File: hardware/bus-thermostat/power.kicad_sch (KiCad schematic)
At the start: 14 parts, among them SW1 SW_Push, U4 NCP565D2T33R4G, U5 MAX6420UK33+T, U6 TLV9301IDCK

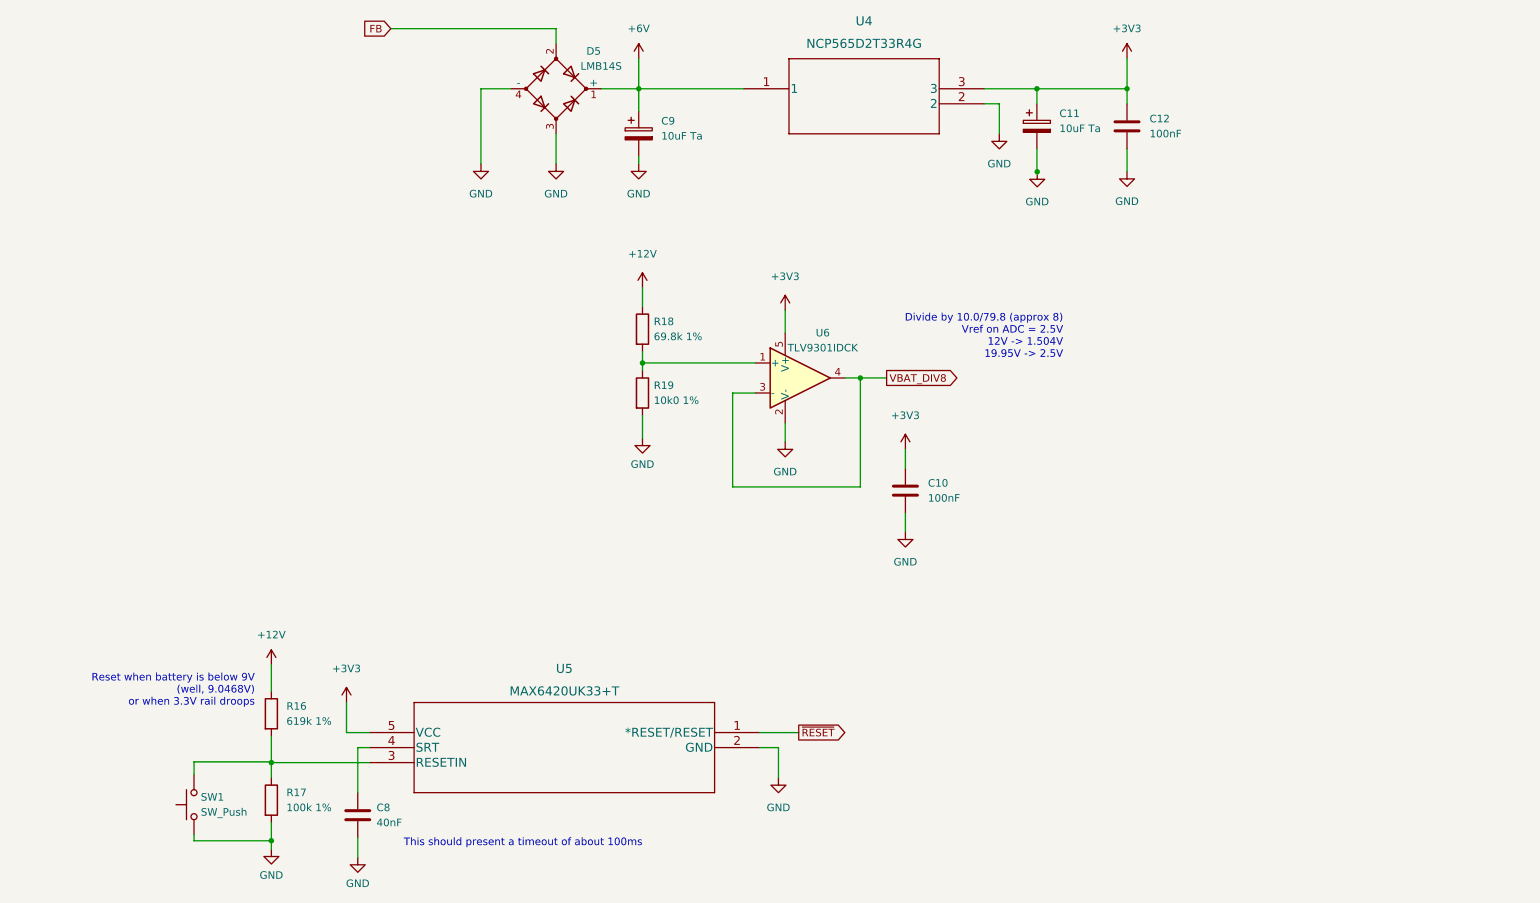
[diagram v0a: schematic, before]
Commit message: Redid the 24VAC path entirely.
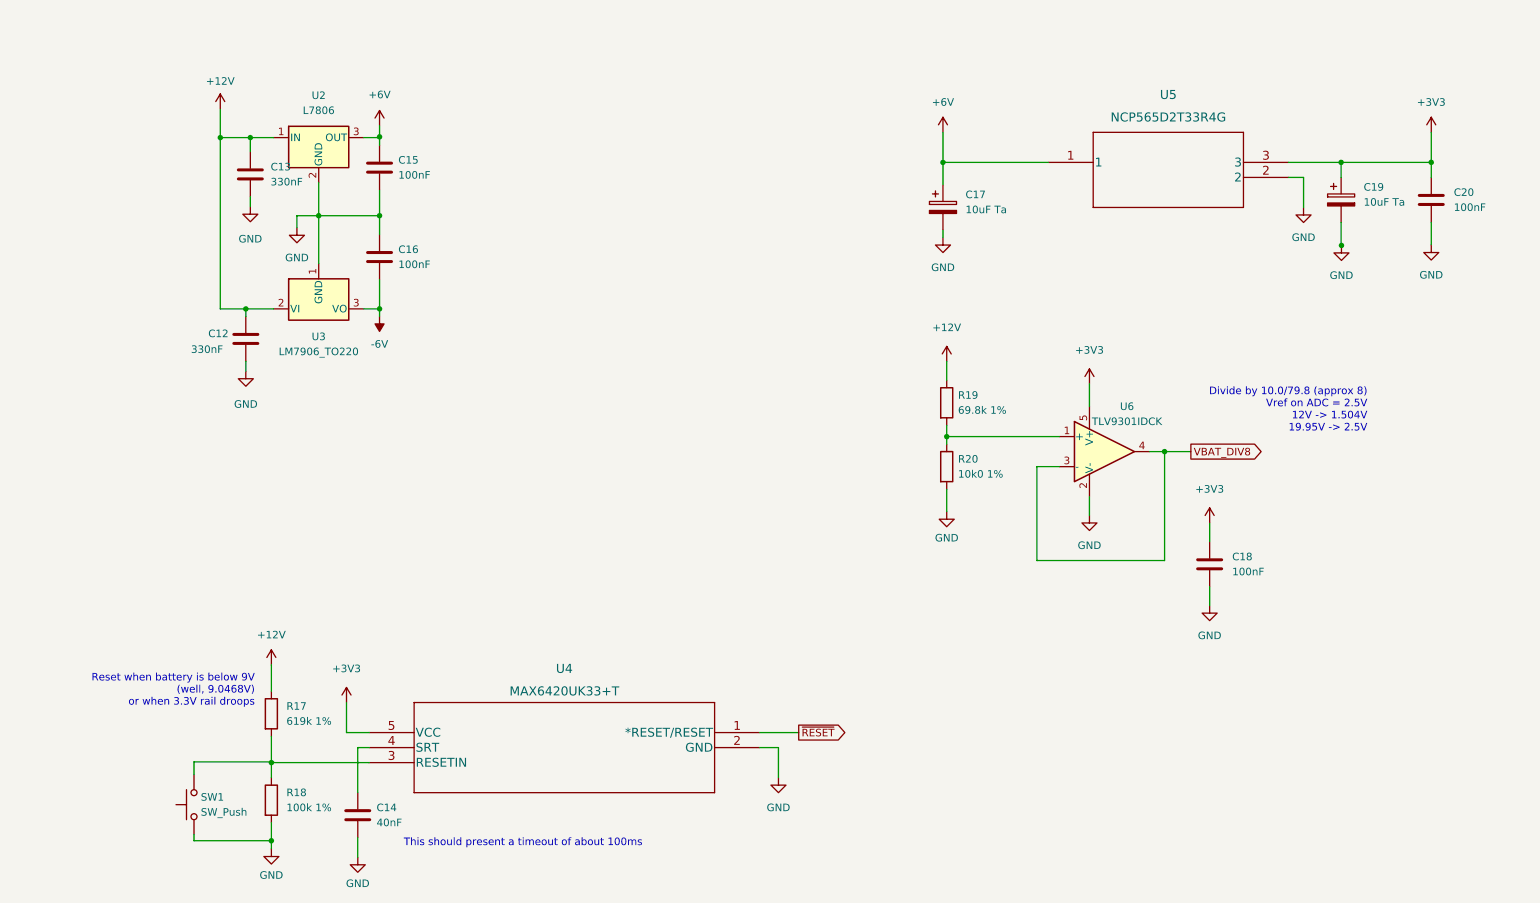
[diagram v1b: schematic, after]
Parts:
- removed D5: LMB14S, Diode_SMD:Diode_Bridge_OnSemi_SDIP-4L, symbol Device:D_Bridge_+AA-
- added C12, C13: 330nF, symbol Device:C
- added C15, C16: 100nF, symbol Device:C
- added U2: L7806, Package_TO_SOT_THT:TO-220-3_Vertical, symbol Regulator_Linear:L7806
- added U3: LM7906_TO220, Package_TO_SOT_THT:TO-220-3_Vertical, symbol Regulator_Linear:LM7906_TO220
- renumbered C8 to C14, C9 to C17, C10 to C18, C11 to C19, C12 to C20, R16 to R17, R17 to R18, R18 to R19, R19 to R20, U5 to U4, U4 to U5
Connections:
- net +12V: now also C12.1, C13.1, U2.1 (IN), U3.2 (VI)
- net GND: now also C12.2, C13.2, C15.2, C16.1, U2.2 (GND), U3.1 (GND)
- new net: C15.1, U2.3 (OUT)
- new net -6V: C16.2, U3.3 (VO)
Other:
- moved on the sheet: C17, C18, C19, C20, R19, R20, U5, U6

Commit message: First rev of thermostat firmware
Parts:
- added D?: 18V Zener, symbol Device:D_Zener
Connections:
- net GND: now also D?.2 (A)
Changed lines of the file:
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@@
   (junction (at 78.105 53.213) (diameter 0) (color 0 0 0 0)
   )
+  (junction (at 51.054 40.005) (diameter 0) (color 0 0 0 0)
+  )
   (junction (at 173.355 44.196) (diameter 0) (color 0 0 0 0)
   )
@@
     (stroke (width 0) (type default) (color 0 0 0 0))
   )
+  (wire (pts (xy 38.354 52.959) (xy 38.354 54.991))
+    (stroke (width 0) (type default) (color 0 0 0 0))
+  )
   (wire (pts (xy 210.82 111.506) (xy 210.82 93.091))
     (stroke (width 0) (type default) (color 0 0 0 0))
@@
     (stroke (width 0) (type default) (color 0 0 0 0))
   )
+  (wire (pts (xy 38.354 40.005) (xy 51.054 40.005))
+    (stroke (width 0) (type default) (color 0 0 0 0))
+  )
   (wire (pts (xy 240.665 54.356) (xy 240.665 58.166))
     (stroke (width 0) (type default) (color 0 0 0 0))
@@
   )
   (wire (pts (xy 255.905 54.356) (xy 255.905 58.166))
+    (stroke (width 0) (type default) (color 0 0 0 0))
+  )
+  (wire (pts (xy 38.354 40.005) (xy 38.354 45.339))
     (stroke (width 0) (type default) (color 0 0 0 0))
   )
@@
     (pin "1")
     (pin "2")
+  )
+  (symbol (lib_name "GND_2") (lib_id "power:GND") (at 38.354 54.991 0) (unit 1)
+    (in_bom yes) (on_board yes) (fields_autoplaced)
+    (property "Reference" "#PWR?" (id 0) (at 38.354 61.341 0)
+      (effects (font (size 1.27 1.27)) hide)
+    )
+    (property "Value" "GND" (id 1) (at 38.354 59.69 0))
+    (property "Footprint" "" (id 2) (at 38.354 54.991 0)
+      (effects (font (size 1.27 1.27)) hide)
+    )
+    (property "Datasheet" "" (id 3) (at 38.354 54.991 0)
+      (effects (font (size 1.27 1.27)) hide)
+    )
+    (pin "1")
   )
   (symbol (lib_id "Device:R") (at 173.99 84.836 0) (unit 1)
@@
     (pin "1")
   )
+  (symbol (lib_id "Device:D_Zener") (at 38.354 49.149 270) (unit 1)
+    (in_bom yes) (on_board yes) (fields_autoplaced)
+    (property "Reference" "D?" (id 0) (at 40.64 47.8789 90)
+      (effects (font (size 1.27 1.27)) (justify left))
+    )
+    (property "Value" "18V Zener" (id 1) (at 40.64 50.4189 90)
+      (effects (font (size 1.27 1.27)) (justify left))
+    )
+    (property "Footprint" "" (id 2) (at 38.354 49.149 0)
+      (effects (font (size 1.27 1.27)) hide)
+    )
+    (property "Datasheet" "~" (id 3) (at 38.354 49.149 0)
+      (effects (font (size 1.27 1.27)) hide)
+    )
+    (pin "1")
+    (pin "2")
+  )
   (symbol (lib_id "power:GND") (at 74.422 161.671 0) (mirror y) (unit 1)

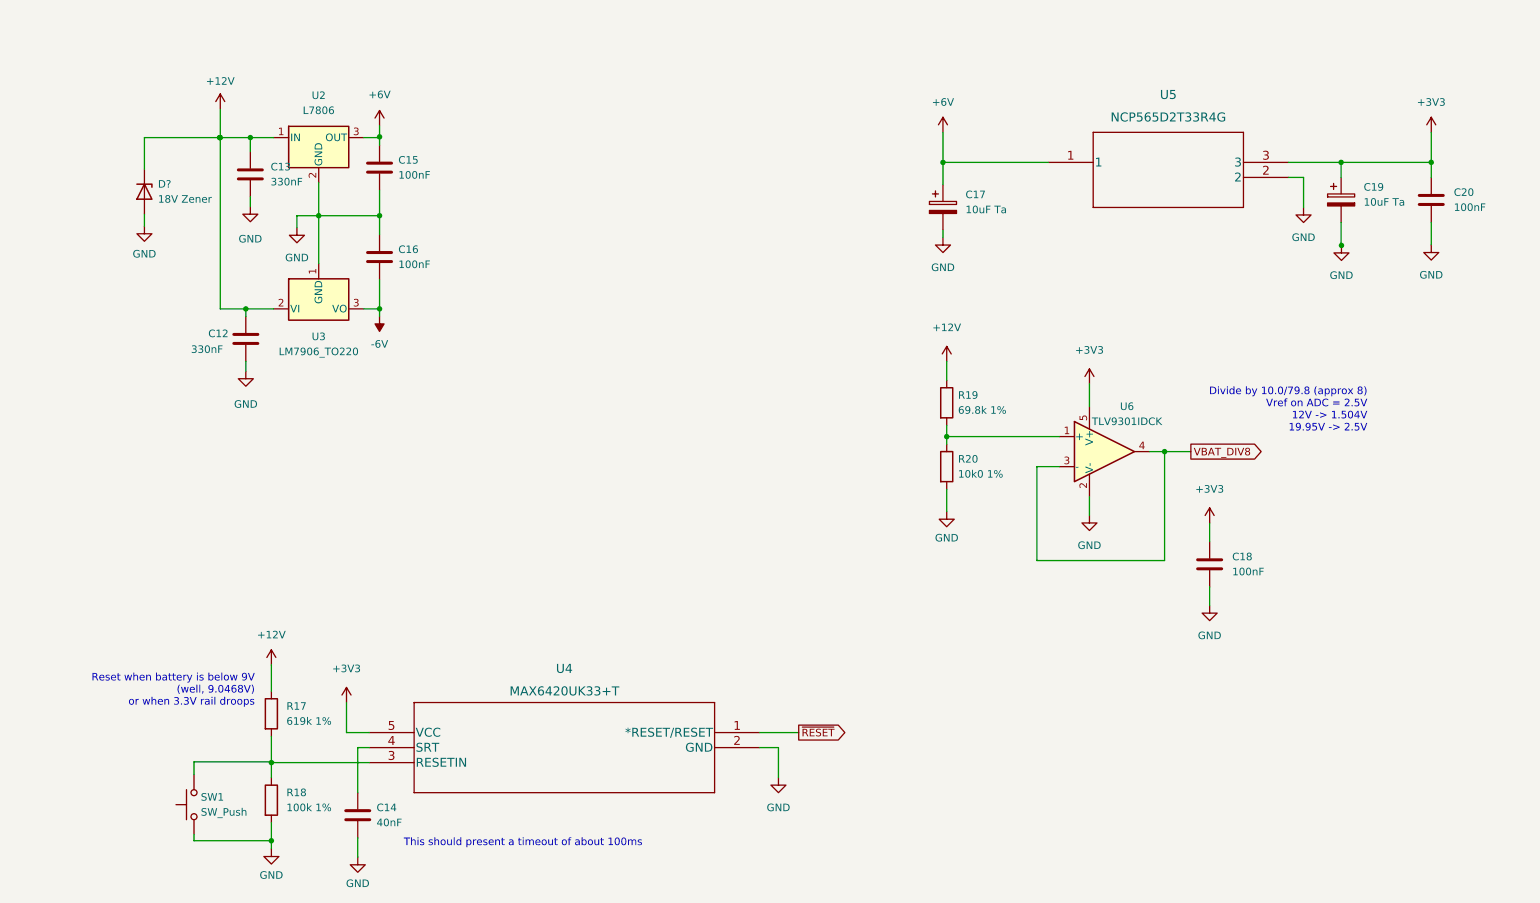
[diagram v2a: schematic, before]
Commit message: Rework the AC path generation again. Opamps only.
- awaiting the completion of analog circuit analysis
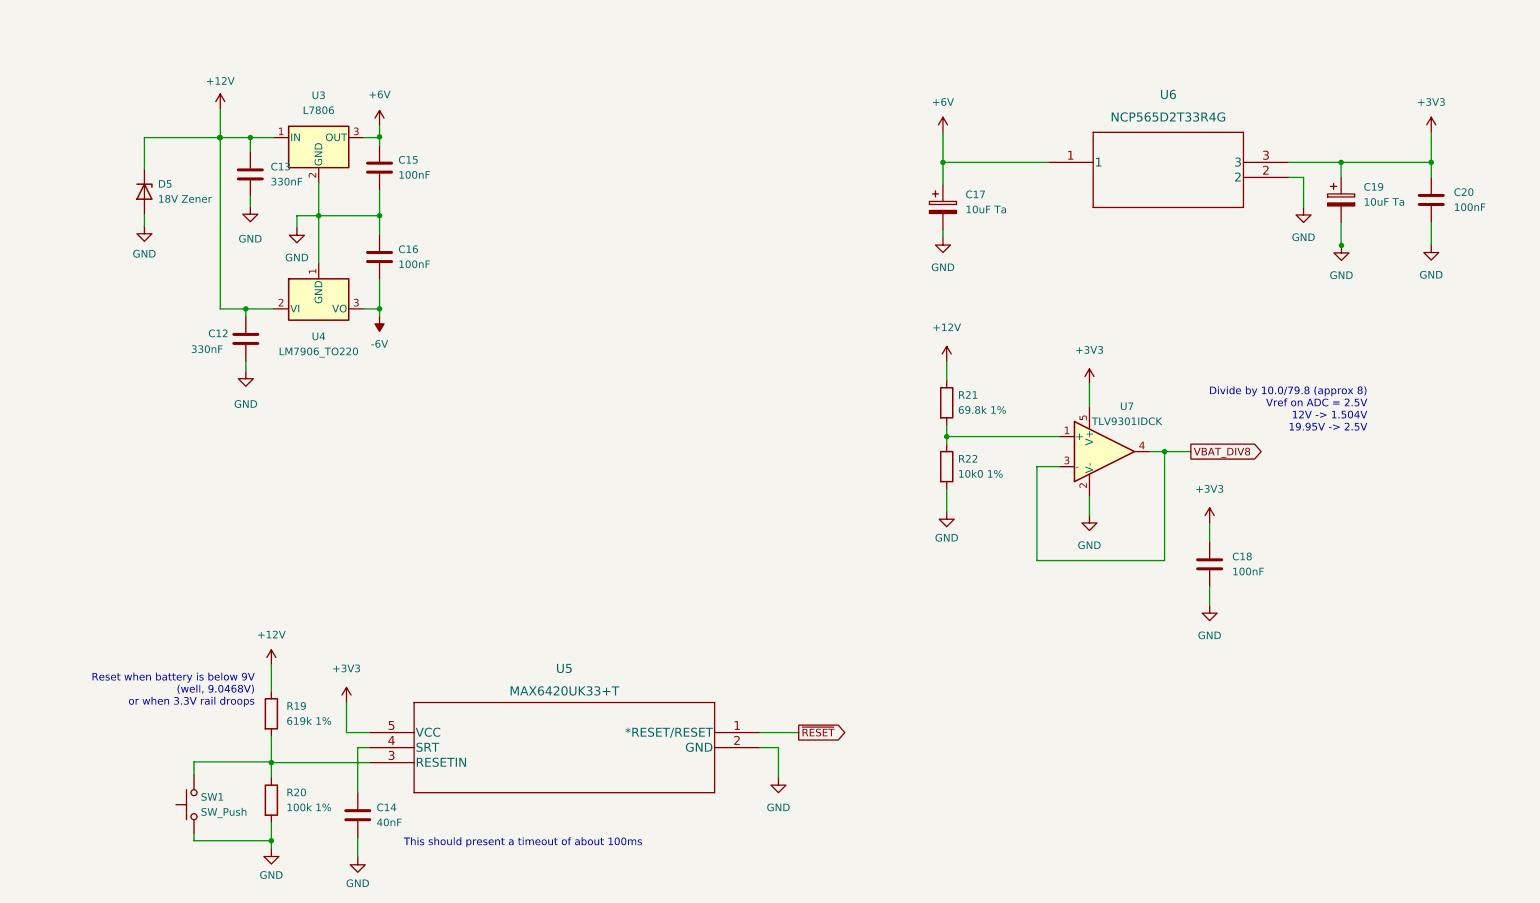
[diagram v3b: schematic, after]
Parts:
- gave numbers to parts that had none: 1
- renumbered R17 to R19, R18 to R20, R19 to R21, R20 to R22, U2 to U3, U3 to U4, U4 to U5, U5 to U6, U6 to U7

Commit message: Update some components
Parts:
- added F1: 6A Polyfuse, Resistor_SMD:R_0603_1608Metric_Pad0.98x0.95mm_HandSolder, symbol Device:Polyfuse
- D5: footprint (none) -> Diode_SMD:D_SOD-123
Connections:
- net at D5.1 (K): now also F1.2
- new net +BATT: F1.1

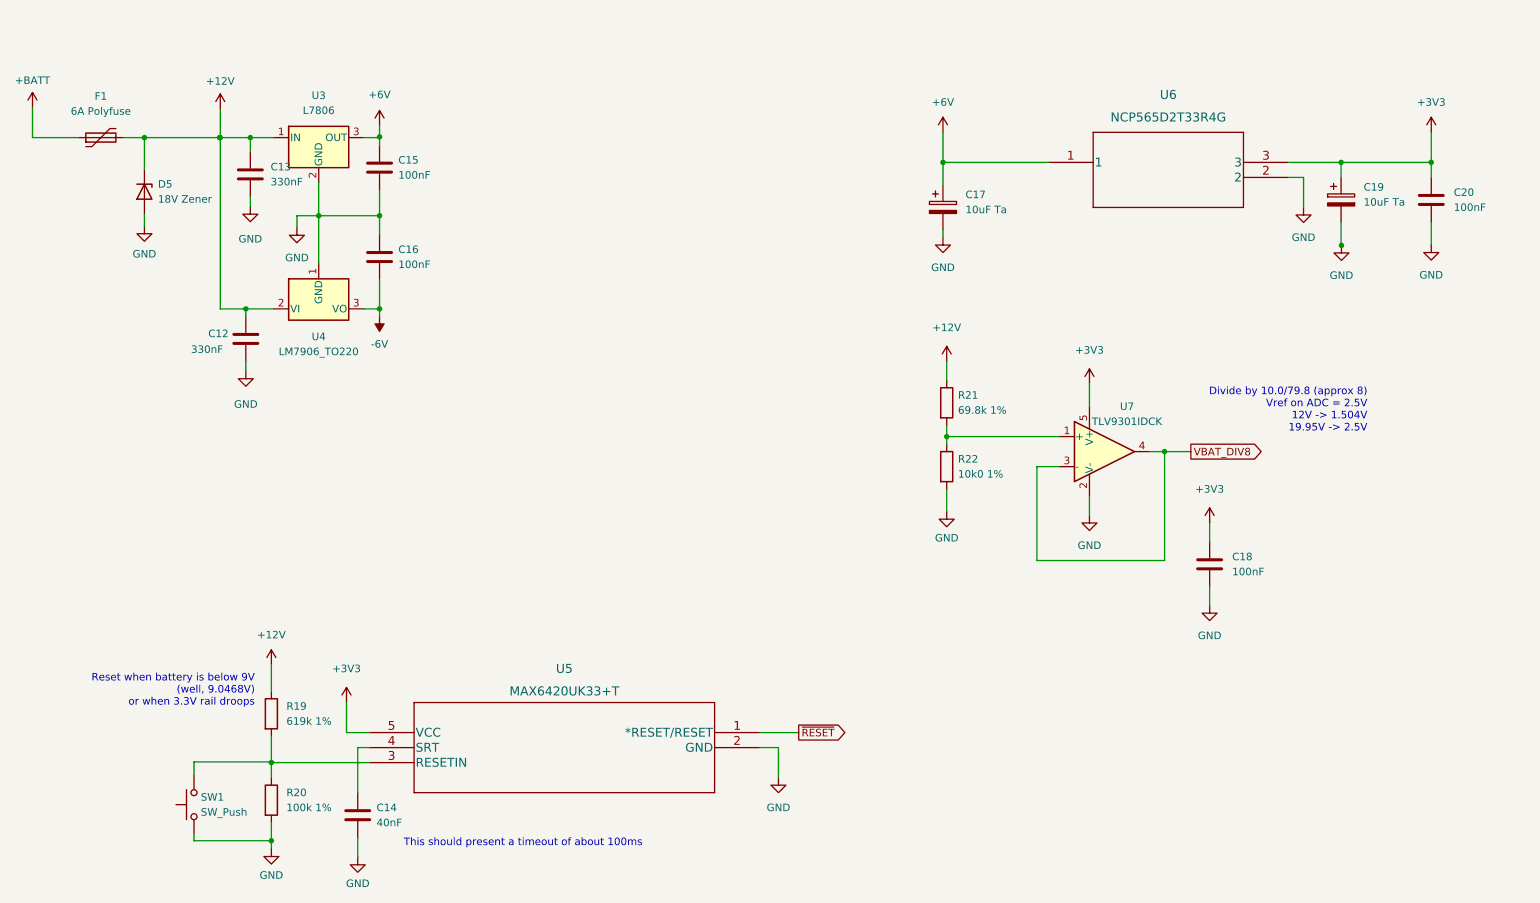
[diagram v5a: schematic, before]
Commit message: Fix oscillator, add fan controller/thermostat and its IOs.
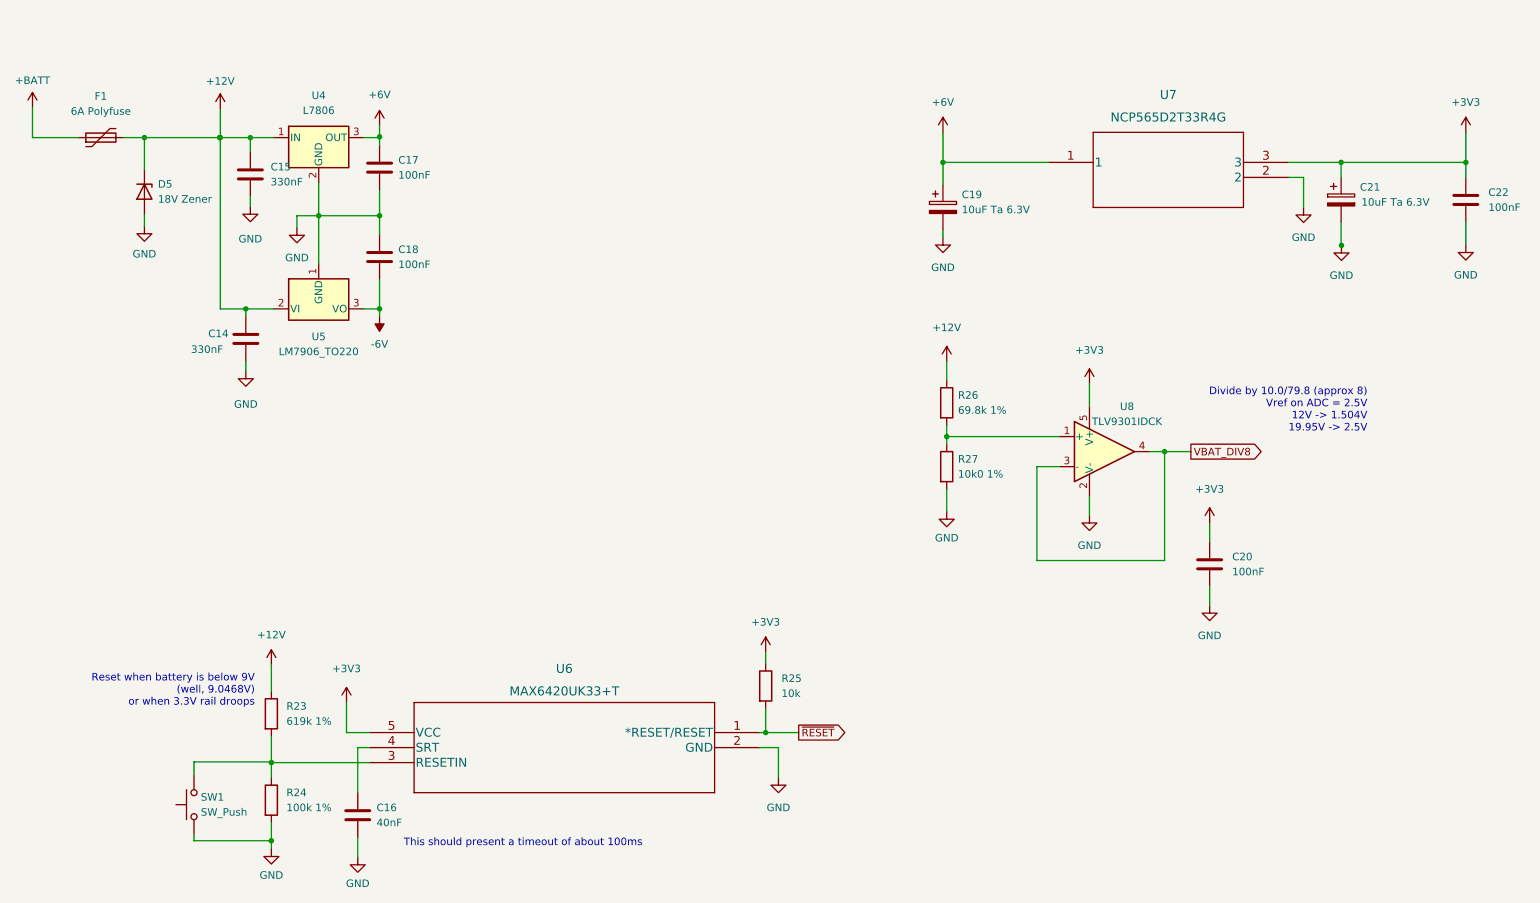
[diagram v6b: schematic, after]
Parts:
- added R25: 10k, Resistor_SMD:R_0805_2012Metric_Pad1.20x1.40mm_HandSolder, symbol Device:R
- C14: renamed from C12; footprint (none) -> Capacitor_SMD:C_0805_2012Metric_Pad1.18x1.45mm_HandSolder
- C15: renamed from C13; footprint (none) -> Capacitor_SMD:C_0805_2012Metric_Pad1.18x1.45mm_HandSolder
- C16: renamed from C14; footprint (none) -> Capacitor_SMD:C_0805_2012Metric_Pad1.18x1.45mm_HandSolder
- C17: renamed from C15; footprint (none) -> Capacitor_SMD:C_0805_2012Metric_Pad1.18x1.45mm_HandSolder
- C18: renamed from C16; footprint (none) -> Capacitor_SMD:C_0805_2012Metric_Pad1.18x1.45mm_HandSolder
- C19: renamed from C17; value 10uF Ta -> 10uF Ta 6.3V; footprint (none) -> Capacitor_Tantalum_SMD:CP_EIA-3216-18_Kemet-A_Pad1.58x1.35mm_HandSolder
- C20: renamed from C18; footprint (none) -> Capacitor_SMD:C_0805_2012Metric_Pad1.18x1.45mm_HandSolder
- C21: renamed from C19; value 10uF Ta -> 10uF Ta 6.3V; footprint (none) -> Capacitor_Tantalum_SMD:CP_EIA-3216-18_Kemet-A_Pad1.58x1.35mm_HandSolder
- C22: renamed from C20; footprint (none) -> Capacitor_SMD:C_0805_2012Metric_Pad1.18x1.45mm_HandSolder
- R23: renamed from R19; footprint (none) -> Resistor_SMD:R_0805_2012Metric_Pad1.20x1.40mm_HandSolder
- R24: renamed from R20; footprint (none) -> Resistor_SMD:R_0805_2012Metric_Pad1.20x1.40mm_HandSolder
- R26: renamed from R21; footprint (none) -> Resistor_SMD:R_0805_2012Metric_Pad1.20x1.40mm_HandSolder
- R27: renamed from R22; footprint (none) -> Resistor_SMD:R_0805_2012Metric_Pad1.20x1.40mm_HandSolder
- SW1: footprint (none) -> SparkFun-Switches:TACTILE_SWITCH_PTH_6.0MM
- renumbered U3 to U4, U4 to U5, U5 to U6, U6 to U7, U7 to U8
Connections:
- net +3V3: now also R25.1
- net ~{RESET}: now also R25.2
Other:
- moved on the sheet: C22
